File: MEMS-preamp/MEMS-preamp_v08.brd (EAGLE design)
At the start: 51 x 30 mm, 49 parts, among them IC1 BQ297X, IC2 OPA2134UA, IC3 MCP73831, IC4 SC4503, IC5 TPS7A49, IC6 QS6K1, J5 Battery, SW3 SPDT

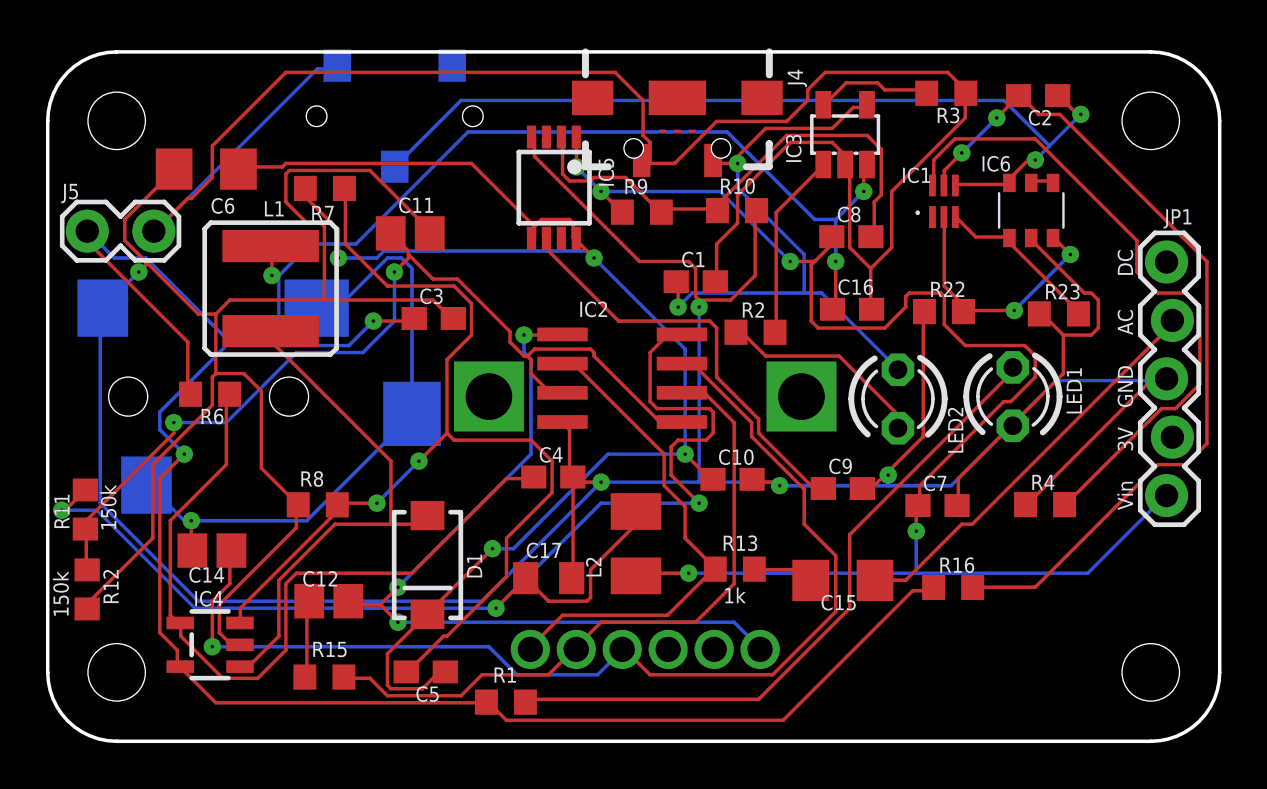
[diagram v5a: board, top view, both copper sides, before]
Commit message: MEMS preamp with electrolytic caps
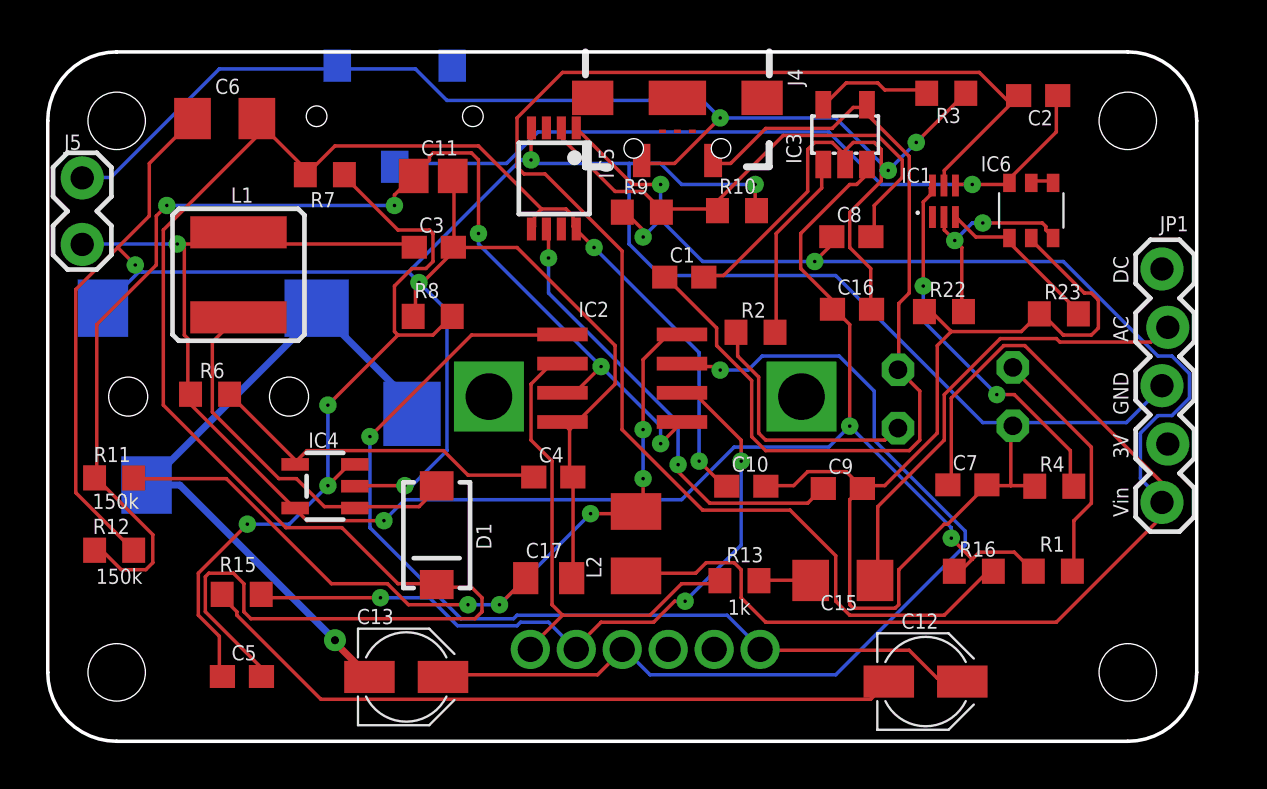
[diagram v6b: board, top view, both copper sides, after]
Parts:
- removed C14: 10uF, adafruit:C0805
- added C13: 10uF, resistor:PANASONIC_B
- C12: device adafruit:C0805 -> resistor:PANASONIC_B
- J3: value (none) -> TRS-1/8"-3.5MM
- moved C12 26.2 mm to (38.2, 2.60), turned to 0 degrees
- moved R1 24.5 mm to (43.7, 7.40)
- moved R8 9.60 mm to (16.8, 18.5)
- moved IC4 8.52 mm to (12.1, 11.1)
- moved C5 8.00 mm to (8.45, 2.82)
- moved R15 5.09 mm to (8.44, 6.39)
- moved C3 3.10 mm to (16.8, 21.5)
- moved C11 2.69 mm to (16.8, 24.6)
- moved C6 2.34 mm to (7.70, 27.1)
- moved R12 2.07 mm to (2.89, 8.31), turned to 180 degrees
- moved R11 1.86 mm to (2.89, 11.5), turned to 0 degrees
- moved C7 1.58 mm to (40.0, 11.2)
- moved L1 1.52 mm to (8.30, 20.3)
- moved D1 1.36 mm to (16.9, 8.97)
- moved R16 1.14 mm to (40.3, 7.40)
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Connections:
- net N$10: now also C13.+; no longer C14.1
- net N$4: now also C12.-; no longer C12.2
- net N$7: now also C13.-; no longer C14.2
- net N$9: now also C12.+; no longer C12.1
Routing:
- net VBAT: track 118.5 -> 80.4 mm, vias 5 -> 4
- net N$42: track 37.1 -> 66.1 mm, vias 2 -> 0
- net N$4: track 3.36 -> 31.4 mm
- net GND: track 199.7 -> 175.8 mm
- net +12V: track 67.8 -> 88.1 mm, vias 5 -> 3
- net N$15: track 55.3 -> 36.3 mm, vias 3 -> 5
- net N$2: track 29.3 -> 10.6 mm
- net N$13: track 33.3 -> 15.3 mm
- net V+: track 66.2 -> 83.9 mm, vias 4 -> 2
- net USBGND: track 82.8 -> 69.1 mm, vias 0 -> 3
- net N$8: track 42.0 -> 55.1 mm, vias 2 -> 5
- net +5V: track 27.3 -> 40.1 mm, vias 2 -> 0
- net N$34: track 28.3 -> 16.5 mm, vias 0 -> 2
- net N$14: track 45.0 -> 34.8 mm, vias 2 -> 3
- net N$9: track 35.1 -> 42.9 mm, vias 3 -> 1
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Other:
- board size 51 x 30 mm -> 50 x 30 mm

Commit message: MEMS preamp with electrolytic caps
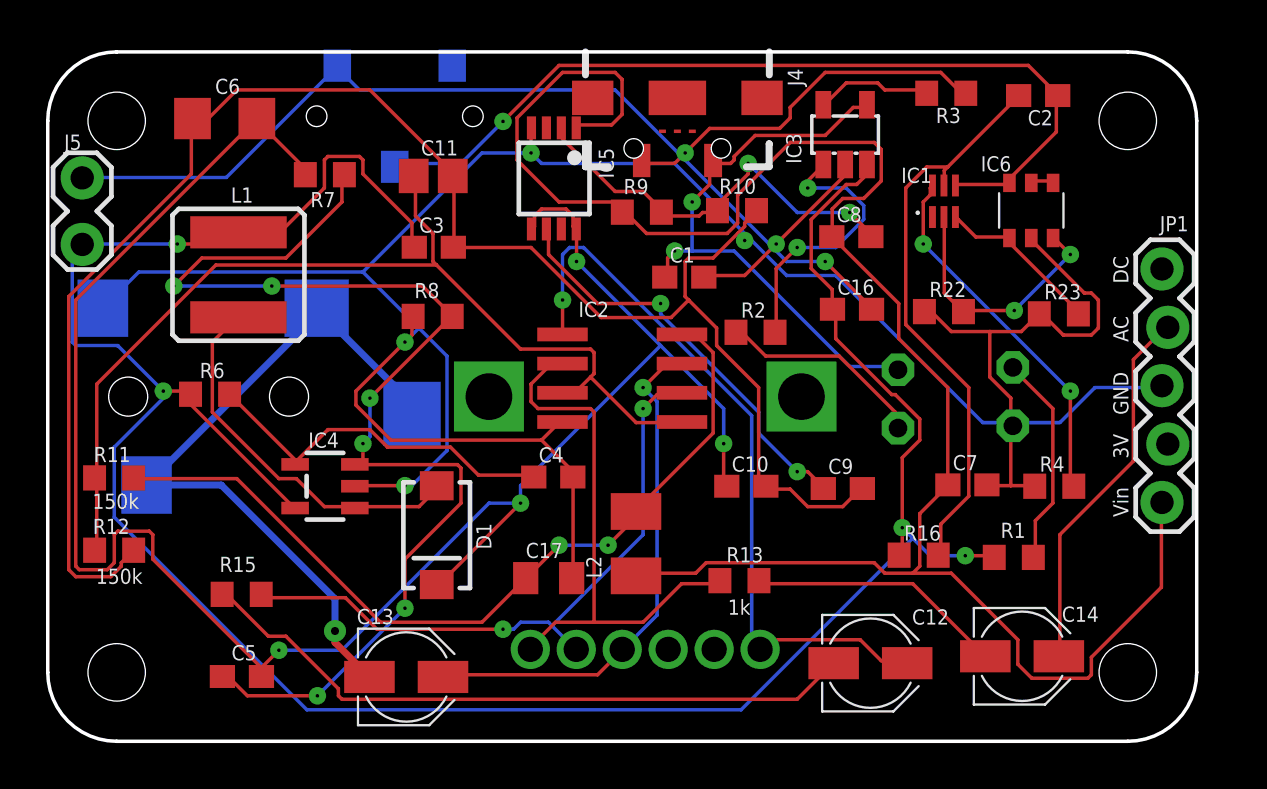
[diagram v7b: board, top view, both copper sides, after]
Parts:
- removed C15: 10uF, rcl:C1206
- added C14: 10uF, resistor:PANASONIC_B
- moved C12 2.53 mm to (35.8, 3.40)
- moved R16 2.50 mm to (37.9, 8.10)
- moved R1 1.80 mm to (42.0, 8.00)
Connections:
- net N$23: now also C14.-; no longer C15.2
- net N$3: now also C14.+; no longer C15.1
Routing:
- net N$42: track 66.1 -> 25.1 mm
- net VBAT: track 80.4 -> 109.6 mm
- net N$10: track 43.8 -> 22.8 mm
- net N$14: track 34.8 -> 52.8 mm, vias 3 -> 6
- net +5V: track 40.1 -> 25.5 mm, vias 0 -> 2
- net GND: track 175.8 -> 190.0 mm, vias 5 -> 4
- net N$9: track 42.9 -> 32.2 mm
- net N$8: track 55.1 -> 44.5 mm, vias 5 -> 0
- net N$23: track 2.25 -> 11.2 mm
- net N$47: track 22.7 -> 18.2 mm, vias 0 -> 2
- net BATGND: track 33.8 -> 38.4 mm
- net N$3: track 20.5 -> 16.3 mm
- net N$25: track 8.17 -> 12.2 mm, vias 0 -> 2
- net N$21: track 32.0 -> 28.1 mm, vias 3 -> 2
- net +12V: track 88.1 -> 85.1 mm, vias 3 -> 0
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
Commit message: gerbers for mems and piezo
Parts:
- moved C14 1.14 mm to (41.7, 2.80)
- moved C12 0.67 mm to (35.5, 2.80)
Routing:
- net N$25: track 12.2 -> 48.0 mm
- net GND: track 190.0 -> 171.7 mm, vias 4 -> 6
- net N$14: track 52.8 -> 41.4 mm, vias 6 -> 4
- net VBAT: track 109.6 -> 99.4 mm
- net N$48: track 18.2 -> 26.3 mm, vias 2 -> 0
- net N$9: track 32.2 -> 27.4 mm
- net N$47: track 18.2 -> 22.3 mm, vias 2 -> 0
- net N$7: track 31.4 -> 33.8 mm
- net +5V: track 25.5 -> 27.6 mm
- net N$22: track 9.15 -> 11.2 mm
- net N$5: track 24.1 -> 22.2 mm
- net N$15: track 36.6 -> 38.5 mm
- net N$31: track 11.2 -> 9.48 mm
- net V+: track 85.4 -> 83.8 mm, vias 4 -> 3
- net N$2: track 9.33 -> 10.8 mm
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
